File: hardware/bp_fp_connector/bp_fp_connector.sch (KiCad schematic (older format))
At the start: 2 parts, among them J1 C96ABC, J2 C96ABC

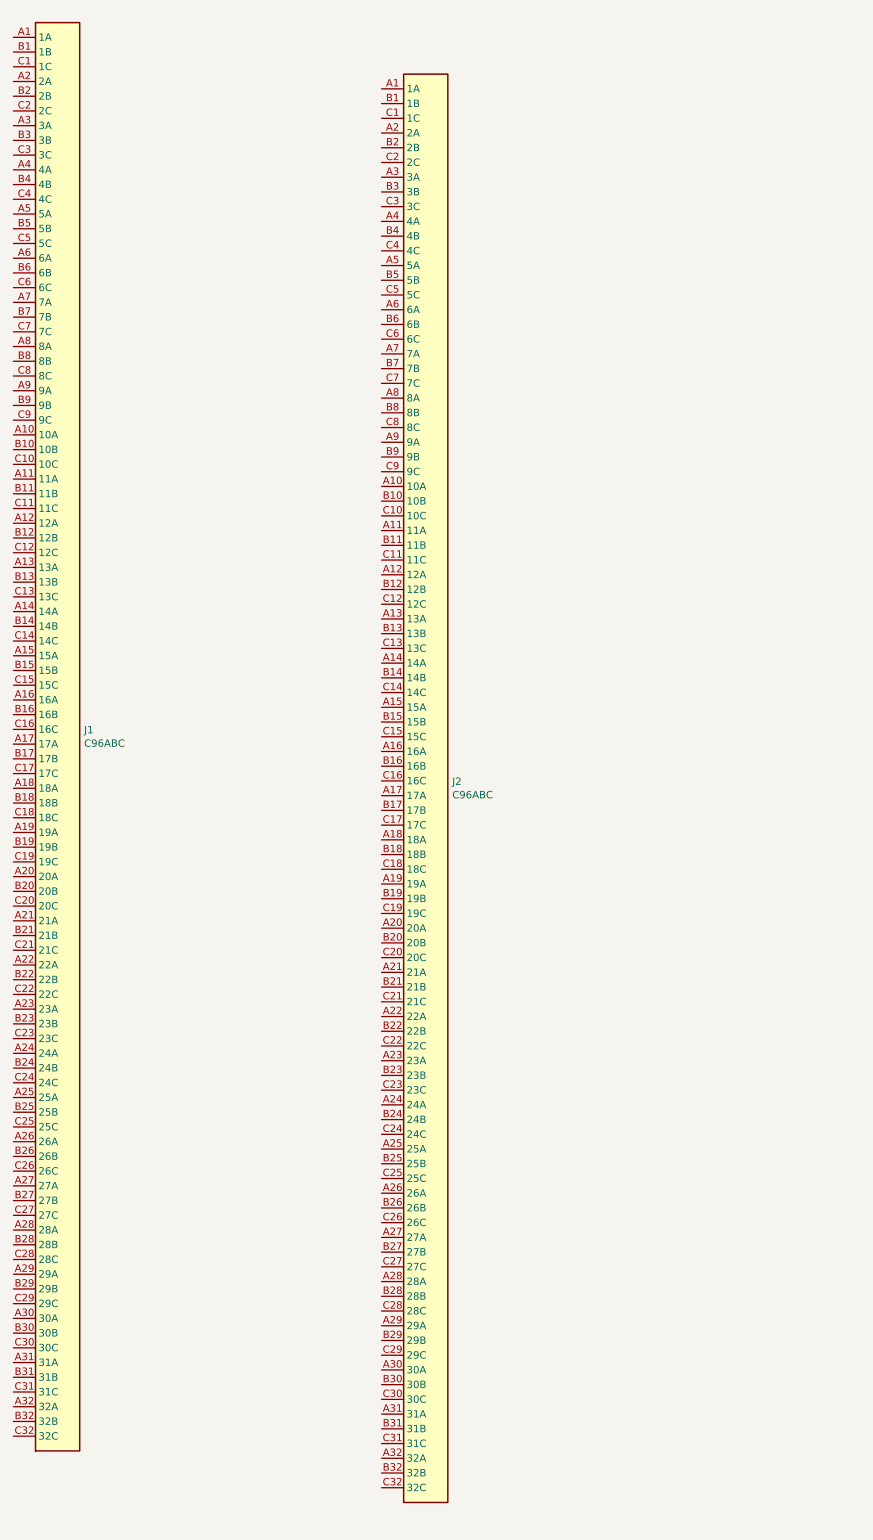
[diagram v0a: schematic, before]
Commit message: front panel - backplane connector
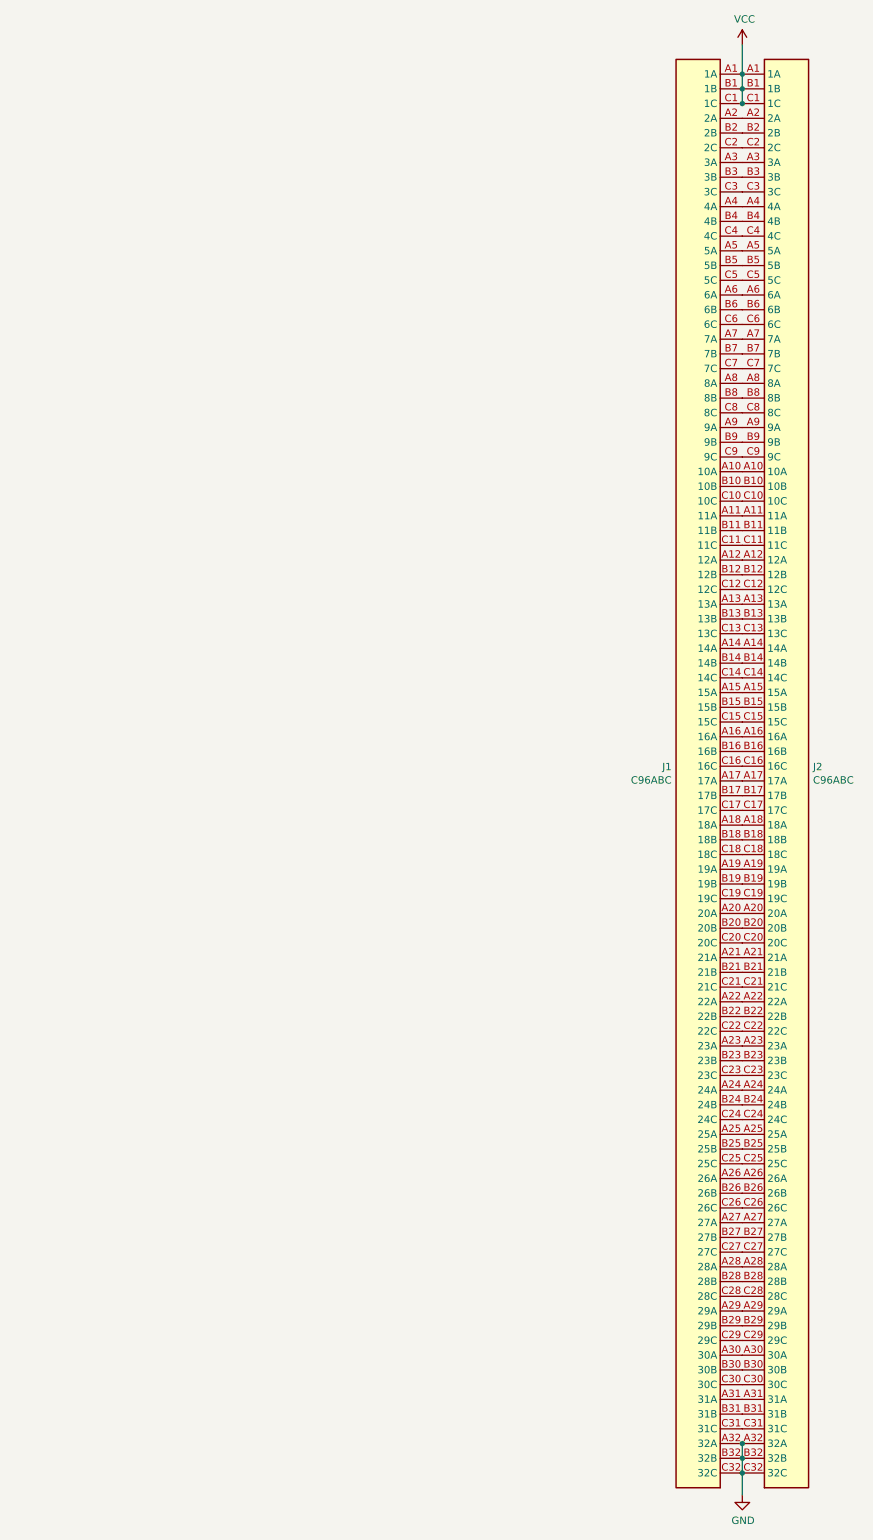
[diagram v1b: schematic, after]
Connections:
- net VCC: now reaches J1.A1 (1A)
- net VCC: now also J1.B1 (1B), J1.C1 (1C), J2.A1 (1A), J2.B1 (1B), J2.C1 (1C)
- net at J1.A10 (10A): now also J2.A10 (10A)
- net at J1.A11 (11A): now also J2.A11 (11A)
- net at J1.A12 (12A): now also J2.A12 (12A)
- net at J1.A13 (13A): now also J2.A13 (13A)
- net at J1.A14 (14A): now also J2.A14 (14A)
- net at J1.A15 (15A): now also J2.A15 (15A)
- net at J1.A16 (16A): now also J2.A16 (16A)
- net at J1.A17 (17A): now also J2.A17 (17A)
- net at J1.A18 (18A): now also J2.A18 (18A)
- net at J1.A19 (19A): now also J2.A19 (19A)
- net at J1.A2 (2A): now also J2.A2 (2A)
- net at J1.A20 (20A): now also J2.A20 (20A)
- net at J1.A21 (21A): now also J2.A21 (21A)
- net at J1.A22 (22A): now also J2.A22 (22A)
- net at J1.A23 (23A): now also J2.A23 (23A)
- net at J1.A24 (24A): now also J2.A24 (24A)
- net at J1.A25 (25A): now also J2.A25 (25A)
- net at J1.A26 (26A): now also J2.A26 (26A)
- net at J1.A27 (27A): now also J2.A27 (27A)
- net at J1.A28 (28A): now also J2.A28 (28A)
- net at J1.A29 (29A): now also J2.A29 (29A)
- net at J1.A3 (3A): now also J2.A3 (3A)
- net at J1.A30 (30A): now also J2.A30 (30A)
- net at J1.A31 (31A): now also J2.A31 (31A)
- net GND: now reaches J1.A32 (32A)
- net GND: now also J1.B32 (32B), J1.C32 (32C), J2.A32 (32A), J2.B32 (32B), J2.C32 (32C)
- net at J1.A4 (4A): now also J2.A4 (4A)
- net at J1.A5 (5A): now also J2.A5 (5A)
- net at J1.A6 (6A): now also J2.A6 (6A)
- net at J1.A7 (7A): now also J2.A7 (7A)
- net at J1.A8 (8A): now also J2.A8 (8A)
- net at J1.A9 (9A): now also J2.A9 (9A)
- net at J1.B10 (10B): now also J2.B10 (10B)
- net at J1.B11 (11B): now also J2.B11 (11B)
- net at J1.B12 (12B): now also J2.B12 (12B)
- net at J1.B13 (13B): now also J2.B13 (13B)
- net at J1.B14 (14B): now also J2.B14 (14B)
- net at J1.B15 (15B): now also J2.B15 (15B)
- net at J1.B16 (16B): now also J2.B16 (16B)
- net at J1.B17 (17B): now also J2.B17 (17B)
- net at J1.B18 (18B): now also J2.B18 (18B)
- net at J1.B19 (19B): now also J2.B19 (19B)
- net at J1.B2 (2B): now also J2.B2 (2B)
- net at J1.B20 (20B): now also J2.B20 (20B)
- net at J1.B21 (21B): now also J2.B21 (21B)
- net at J1.B22 (22B): now also J2.B22 (22B)
- net at J1.B23 (23B): now also J2.B23 (23B)
- net at J1.B24 (24B): now also J2.B24 (24B)
- net at J1.B25 (25B): now also J2.B25 (25B)
- net at J1.B26 (26B): now also J2.B26 (26B)
- net at J1.B27 (27B): now also J2.B27 (27B)
- net at J1.B28 (28B): now also J2.B28 (28B)
- net at J1.B29 (29B): now also J2.B29 (29B)
- net at J1.B3 (3B): now also J2.B3 (3B)
- net at J1.B30 (30B): now also J2.B30 (30B)
- net at J1.B31 (31B): now also J2.B31 (31B)
- net at J1.B4 (4B): now also J2.B4 (4B)
- net at J1.B5 (5B): now also J2.B5 (5B)
- net at J1.B6 (6B): now also J2.B6 (6B)
- net at J1.B7 (7B): now also J2.B7 (7B)
- net at J1.B8 (8B): now also J2.B8 (8B)
- net at J1.B9 (9B): now also J2.B9 (9B)
- net at J1.C10 (10C): now also J2.C10 (10C)
- net at J1.C11 (11C): now also J2.C11 (11C)
- net at J1.C12 (12C): now also J2.C12 (12C)
- net at J1.C13 (13C): now also J2.C13 (13C)
- net at J1.C14 (14C): now also J2.C14 (14C)
- net at J1.C15 (15C): now also J2.C15 (15C)
- net at J1.C16 (16C): now also J2.C16 (16C)
- net at J1.C17 (17C): now also J2.C17 (17C)
- net at J1.C18 (18C): now also J2.C18 (18C)
- net at J1.C19 (19C): now also J2.C19 (19C)
- net at J1.C2 (2C): now also J2.C2 (2C)
- net at J1.C20 (20C): now also J2.C20 (20C)
- net at J1.C21 (21C): now also J2.C21 (21C)
- net at J1.C22 (22C): now also J2.C22 (22C)
- net at J1.C23 (23C): now also J2.C23 (23C)
- net at J1.C24 (24C): now also J2.C24 (24C)
- net at J1.C25 (25C): now also J2.C25 (25C)
- net at J1.C26 (26C): now also J2.C26 (26C)
- net at J1.C27 (27C): now also J2.C27 (27C)
- net at J1.C28 (28C): now also J2.C28 (28C)
- net at J1.C29 (29C): now also J2.C29 (29C)
- net at J1.C3 (3C): now also J2.C3 (3C)
- net at J1.C30 (30C): now also J2.C30 (30C)
- net at J1.C31 (31C): now also J2.C31 (31C)
- net at J1.C4 (4C): now also J2.C4 (4C)
- net at J1.C5 (5C): now also J2.C5 (5C)
- net at J1.C6 (6C): now also J2.C6 (6C)
- net at J1.C7 (7C): now also J2.C7 (7C)
- net at J1.C8 (8C): now also J2.C8 (8C)
- net at J1.C9 (9C): now also J2.C9 (9C)
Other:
- moved on the sheet: J1, J2
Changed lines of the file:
@@
 $EndDescr
+$Comp
+L Connector:C96ABC J2
+U 1 1 620876F9
+P 7900 4650
+F 0 "J2" H 8080 4746 50  0000 L CNN
+F 1 "C96ABC" H 8080 4655 50  0000 L CNN
+F 2 "din61412:DIN41612_C_3x32_Male_Horizontal_THT_CAPS" H 7900 4700 50  0001 C CNN
+F 3 " ~" H 7900 4700 50  0001 C CNN
+	1    7900 4650
+	1    0    0    -1
+$EndComp
+$Comp
+L power:VCC #PWR?
+U 1 1 620AF034
+P 7600 -350
+F 0 "#PWR?" H 7600 -500 50  0001 C CNN
+F 1 "VCC" H 7615 -177 50  0000 C CNN
+F 2 "" H 7600 -350 50  0001 C CNN
+F 3 "" H 7600 -350 50  0001 C CNN
+	1    7600 -350
+	1    0    0    -1
+$EndComp
+$Comp
+L power:GND #PWR?
+U 1 1 620AFB6A
+P 7600 9500
+F 0 "#PWR?" H 7600 9250 50  0001 C CNN
+F 1 "GND" H 7605 9327 50  0000 C CNN
+F 2 "" H 7600 9500 50  0001 C CNN
+F 3 "" H 7600 9500 50  0001 C CNN
+	1    7600 9500
+	1    0    0    -1
+$EndComp
 $Comp
 L Connector:C96ABC J1
 U 1 1 620848F4
-P 2950 4400
-F 0 "J1" H 3130 4496 50  0000 L CNN
-F 1 "C96ABC" H 3130 4405 50  0000 L CNN
-F 2 "din61412:DIN41612_C_3x32_Male_Horizontal_THT_CAPS" H 2950 4450 50  0001 C CNN
-F 3 " ~" H 2950 4450 50  0001 C CNN
-	1    2950 4400
-	1    0    0    -1
+P 7300 4650
+F 0 "J1" H 7480 4746 50  0000 L CNN
+F 1 "C96ABC" H 7480 4655 50  0000 L CNN
+F 2 "din61412:DIN41612_C_3x32_Male_Horizontal_THT_CAPS" H 7300 4700 50  0001 C CNN
+F 3 " ~" H 7300 4700 50  0001 C CNN
+	1    7300 4650
+	-1   0    0    -1
 $EndComp
-$Comp
-L Connector:C96ABC J2
-U 1 1 620876F9
-P 5450 4750
-F 0 "J2" H 5630 4846 50  0000 L CNN
-F 1 "C96ABC" H 5630 4755 50  0000 L CNN
-F 2 "din61412:DIN41612_C_3x32_Male_Horizontal_THT_CAPS" H 5450 4800 50  0001 C CNN
-F 3 " ~" H 5450 4800 50  0001 C CNN
-	1    5450 4750
-	1    0    0    -1
-$EndComp
+Wire Wire Line
+	7600 9500 7600 9350
+Connection ~ 7600 9150
+Connection ~ 7600 9250
+Wire Wire Line
+	7600 9250 7600 9150
+Connection ~ 7600 9350
+Wire Wire Line
+	7600 9350 7600 9250
+Wire Wire Line
+	7600 -350 7600 -150
+Connection ~ 7600 50
+Connection ~ 7600 -150
+Wire Wire Line
+	7600 -150 7600 -50
+Connection ~ 7600 -50
+Wire Wire Line
+	7600 -50  7600 50
 $EndSCHEMATC
